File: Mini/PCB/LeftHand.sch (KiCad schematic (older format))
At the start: 30 parts

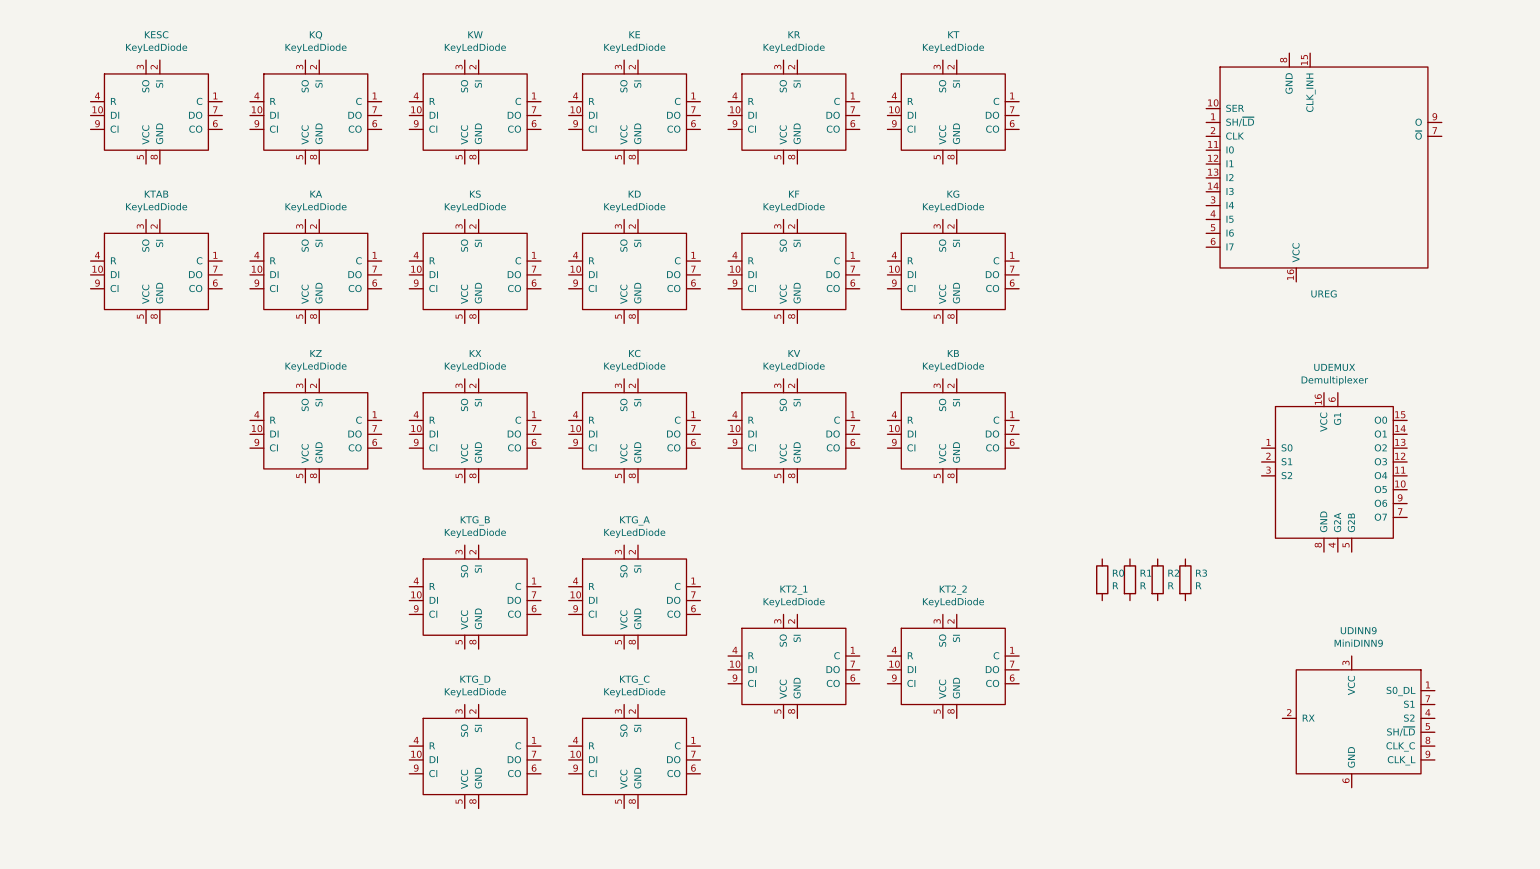
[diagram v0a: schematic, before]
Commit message: Wiring left hand schematic, adding footprints, and generating netlist.
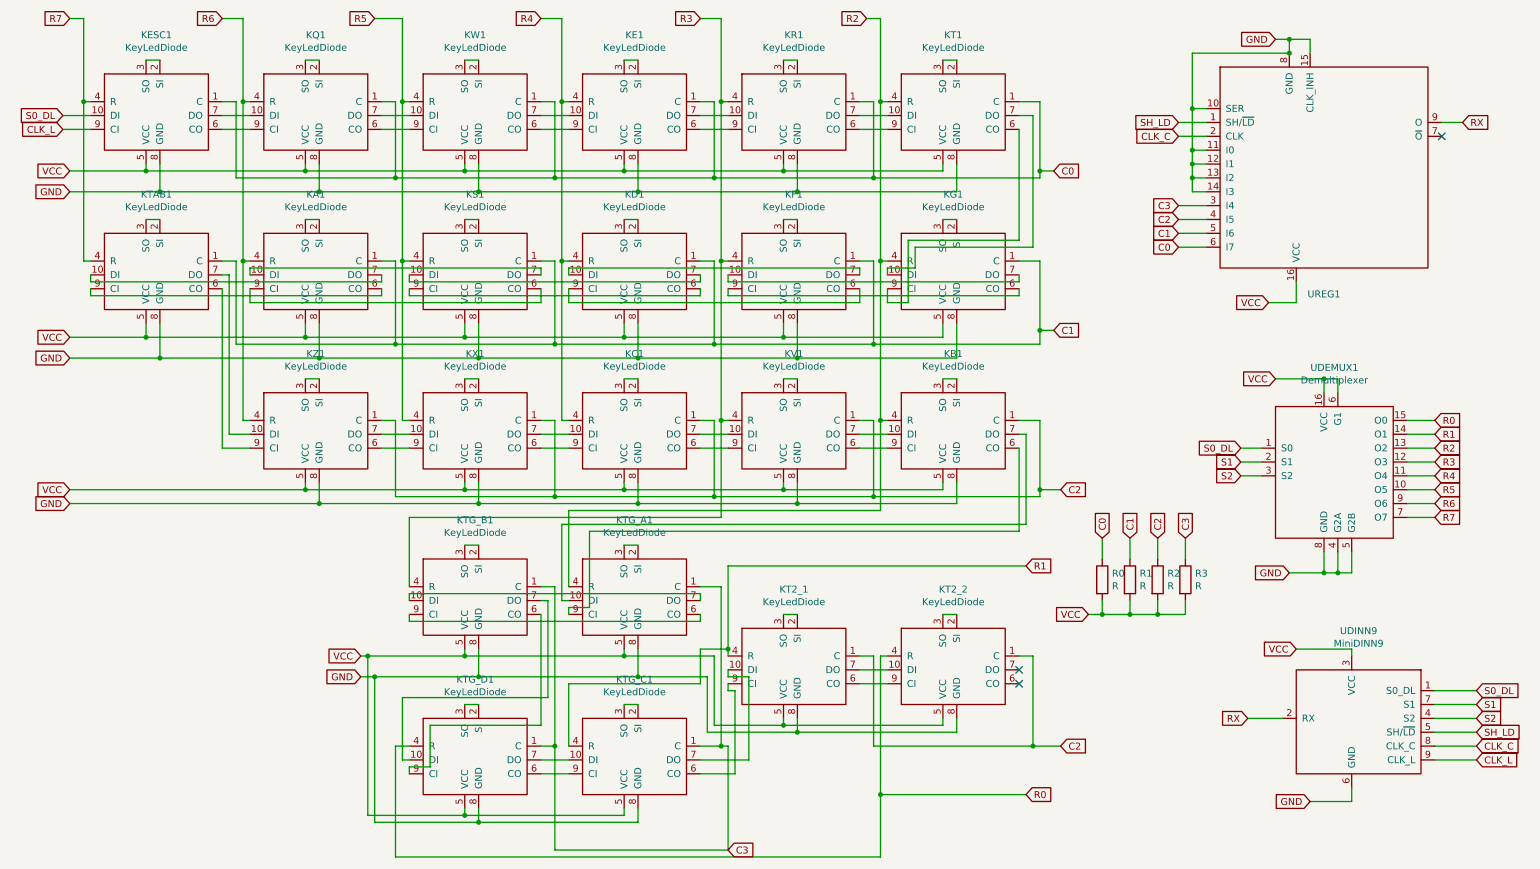
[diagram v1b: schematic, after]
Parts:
- KA1: renamed from KA; footprint (none) -> Mini:KeyLedDiodeR2L
- KB1: renamed from KB; footprint (none) -> Mini:KeyLedDiodeL2R
- KC1: renamed from KC; footprint (none) -> Mini:KeyLedDiodeL2R
- KD1: renamed from KD; footprint (none) -> Mini:KeyLedDiodeR2L
- KE1: renamed from KE; footprint (none) -> Mini:KeyLedDiodeL2R
- KESC1: renamed from KESC; footprint (none) -> Mini:KeyLedDiodeL2R
- KF1: renamed from KF; footprint (none) -> Mini:KeyLedDiodeR2L
- KG1: renamed from KG; footprint (none) -> Mini:KeyLedDiodeR2L
- KQ1: renamed from KQ; footprint (none) -> Mini:KeyLedDiodeL2R
- KR1: renamed from KR; footprint (none) -> Mini:KeyLedDiodeL2R
- KS1: renamed from KS; footprint (none) -> Mini:KeyLedDiodeR2L
- KT1: renamed from KT; footprint (none) -> Mini:KeyLedDiodeL2R
- KT2_1: footprint (none) -> Mini:Key2LedDiodeR2L
- KT2_2: footprint (none) -> Mini:Key2LedDiodeL2R
- KTAB1: renamed from KTAB; footprint (none) -> Mini:KeyLedDiodeR2L
- KTG_A1: renamed from KTG_A; footprint (none) -> Mini:KeyLedDiodeR2L
- KTG_B1: renamed from KTG_B; footprint (none) -> Mini:KeyLedDiodeR2L
- KTG_C1: renamed from KTG_C; footprint (none) -> Mini:KeyLedDiodeL2R
- KTG_D1: renamed from KTG_D; footprint (none) -> Mini:KeyLedDiodeL2R
- KV1: renamed from KV; footprint (none) -> Mini:KeyLedDiodeL2R
- KW1: renamed from KW; footprint (none) -> Mini:KeyLedDiodeL2R
- KX1: renamed from KX; footprint (none) -> Mini:KeyLedDiodeL2R
- KZ1: renamed from KZ; footprint (none) -> Mini:KeyLedDiodeL2R
- R0, R1, R2, R3: footprint (none) -> Mini:PullupResistor
- UDEMUX1: renamed from UDEMUX; footprint (none) -> Mini:DualInlineMicrochip2x8
- UDINN9: footprint (none) -> Mini:MiniDin9
- UREG1: renamed from UREG; footprint (none) -> Mini:DualInlineMicrochip2x8
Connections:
- net S0_DL: now reaches UDINN9.1 (S0_DL)
- net S0_DL: now also KESC1.10 (DI), UDEMUX1.1 (S0)
- net RX: now reaches UDINN9.2 (RX)
- net RX: now also UREG1.9 (O)
- net VCC: now reaches UDINN9.3 (VCC)
- net VCC: now also KA1.5 (VCC), KB1.5 (VCC), KC1.5 (VCC), KD1.5 (VCC), KE1.5 (VCC), KESC1.5 (VCC), KF1.5 (VCC), KG1.5 (VCC), KQ1.5 (VCC), KR1.5 (VCC), KS1.5 (VCC), KT1.5 (VCC), KT2_1.5 (VCC), KT2_2.5 (VCC), KTAB1.5 (VCC), KTG_A1.5 (VCC), KTG_B1.5 (VCC), KTG_C1.5 (VCC), KTG_D1.5 (VCC), KV1.5 (VCC), KW1.5 (VCC), KX1.5 (VCC), KZ1.5 (VCC), R0.2, R1.2, R2.2, R3.2, UDEMUX1.16 (VCC), UDEMUX1.6 (G1), UREG1.16 (VCC)
- net S2: now reaches UDINN9.4 (S2)
- net S2: now also UDEMUX1.3 (S2)
- net SH_LD: now reaches UDINN9.5 (SH/~LD)
- net SH_LD: now also UREG1.1 (SH/~LD)
- net GND: now reaches UDINN9.6 (GND)
- net GND: now also KA1.8 (GND), KB1.8 (GND), KC1.8 (GND), KD1.8 (GND), KE1.8 (GND), KESC1.8 (GND), KF1.8 (GND), KG1.8 (GND), KQ1.8 (GND), KR1.8 (GND), KS1.8 (GND), KT1.8 (GND), KT2_1.8 (GND), KT2_2.8 (GND), KTAB1.8 (GND), KTG_A1.8 (GND), KTG_B1.8 (GND), KTG_C1.8 (GND), KTG_D1.8 (GND), KV1.8 (GND), KW1.8 (GND), KX1.8 (GND), KZ1.8 (GND), UDEMUX1.4 (G2A), UDEMUX1.5 (G2B), UDEMUX1.8 (GND), UREG1.10 (SER), UREG1.11 (I0), UREG1.12 (I1), UREG1.13 (I2), UREG1.14 (I3), UREG1.15 (CLK_INH), UREG1.8 (GND)
- net S1: now reaches UDINN9.7 (S1)
- net S1: now also UDEMUX1.2 (S1)
- net CLK_C: now reaches UDINN9.8 (CLK_C)
- net CLK_C: now also UREG1.2 (CLK)
- net CLK_L: now reaches UDINN9.9 (CLK_L)
- net CLK_L: now also KESC1.9 (CI)
- net R5: now reaches UDEMUX1.10 (O5)
- net R5: now also KS1.4 (R), KW1.4 (R), KX1.4 (R)
- net R4: now reaches UDEMUX1.11 (O4)
- net R4: now also KC1.4 (R), KD1.4 (R), KE1.4 (R)
- net R3: now reaches UDEMUX1.12 (O3)
- net R3: now also KF1.4 (R), KR1.4 (R), KTG_B1.4 (R), KV1.4 (R)
- net R2: now reaches UDEMUX1.13 (O2)
- net R2: now also KB1.4 (R), KG1.4 (R), KT1.4 (R), KTG_A1.4 (R)
- net R1: now reaches UDEMUX1.14 (O1)
- net R1: now also KT2_1.4 (R), KTG_C1.4 (R)
- net R0: now reaches UDEMUX1.15 (O0)
- net R0: now also KT2_2.4 (R), KTG_D1.4 (R)
- net R7: now reaches UDEMUX1.7 (O7)
- net R7: now also KESC1.4 (R), KTAB1.4 (R)
- net R6: now reaches UDEMUX1.9 (O6)
- net R6: now also KA1.4 (R), KQ1.4 (R), KZ1.4 (R)
- net C3: now reaches UREG1.3 (I4)
- net C3: now also KTG_A1.1 (C), KTG_B1.1 (C), KTG_C1.1 (C), KTG_D1.1 (C), R3.1
- net C2: now reaches UREG1.4 (I5)
- net C2: now also KB1.1 (C), KC1.1 (C), KT2_1.1 (C), KT2_2.1 (C), KV1.1 (C), KX1.1 (C), KZ1.1 (C), R2.1
- net C1: now reaches UREG1.5 (I6)
- net C1: now also KA1.1 (C), KD1.1 (C), KF1.1 (C), KG1.1 (C), KS1.1 (C), KTAB1.1 (C), R1.1
- net C0: now reaches UREG1.6 (I7)
- net C0: now also KE1.1 (C), KESC1.1 (C), KQ1.1 (C), KR1.1 (C), KT1.1 (C), KW1.1 (C), R0.1
- net at KESC1.2 (SI): now also KESC1.3 (SO)
- net at KESC1.6 (CO): now also KQ1.9 (CI)
- net at KESC1.7 (DO): now also KQ1.10 (DI)
- net at KQ1.2 (SI): now also KQ1.3 (SO)
- net at KQ1.6 (CO): now also KW1.9 (CI)
- net at KQ1.7 (DO): now also KW1.10 (DI)
- net at KW1.2 (SI): now also KW1.3 (SO)
- net at KW1.6 (CO): now also KE1.9 (CI)
- net at KW1.7 (DO): now also KE1.10 (DI)
- net at KE1.2 (SI): now also KE1.3 (SO)
- net at KE1.6 (CO): now also KR1.9 (CI)
- net at KE1.7 (DO): now also KR1.10 (DI)
- net at KR1.2 (SI): now also KR1.3 (SO)
- net at KR1.6 (CO): now also KT1.9 (CI)
- net at KR1.7 (DO): now also KT1.10 (DI)
- net at KT1.2 (SI): now also KT1.3 (SO)
- net at KT1.6 (CO): now also KG1.9 (CI)
- net at KT1.7 (DO): now also KG1.10 (DI)
- net at KTAB1.10 (DI): now also KA1.7 (DO)
- net at KTAB1.2 (SI): now also KTAB1.3 (SO)
- net at KTAB1.6 (CO): now also KZ1.9 (CI)
- net at KTAB1.7 (DO): now also KZ1.10 (DI)
- net at KTAB1.9 (CI): now also KA1.6 (CO)
- net at KA1.10 (DI): now also KS1.7 (DO)
- net at KA1.2 (SI): now also KA1.3 (SO)
- net at KA1.9 (CI): now also KS1.6 (CO)
- net at KS1.10 (DI): now also KD1.7 (DO)
- net at KS1.2 (SI): now also KS1.3 (SO)
- net at KS1.9 (CI): now also KD1.6 (CO)
- net at KD1.10 (DI): now also KF1.7 (DO)
- net at KD1.2 (SI): now also KD1.3 (SO)
- net at KD1.9 (CI): now also KF1.6 (CO)
- net at KF1.10 (DI): now also KG1.7 (DO)
- net at KF1.2 (SI): now also KF1.3 (SO)
- net at KF1.9 (CI): now also KG1.6 (CO)
- net at KG1.2 (SI): now also KG1.3 (SO)
- net at KZ1.2 (SI): now also KZ1.3 (SO)
- net at KZ1.6 (CO): now also KX1.9 (CI)
- net at KZ1.7 (DO): now also KX1.10 (DI)
- net at KX1.2 (SI): now also KX1.3 (SO)
- net at KX1.6 (CO): now also KC1.9 (CI)
- net at KX1.7 (DO): now also KC1.10 (DI)
- net at KC1.2 (SI): now also KC1.3 (SO)
- net at KC1.6 (CO): now also KV1.9 (CI)
- net at KC1.7 (DO): now also KV1.10 (DI)
- net at KV1.2 (SI): now also KV1.3 (SO)
- net at KV1.6 (CO): now also KB1.9 (CI)
- net at KV1.7 (DO): now also KB1.10 (DI)
- net at KB1.2 (SI): now also KB1.3 (SO)
- net at KB1.6 (CO): now also KTG_A1.9 (CI)
- net at KB1.7 (DO): now also KTG_A1.10 (DI)
- net at KT2_2.10 (DI): now also KT2_1.7 (DO)
- net at KT2_2.2 (SI): now also KT2_2.3 (SO)
- net at KT2_2.9 (CI): now also KT2_1.6 (CO)
- net at KT2_1.10 (DI): now also KTG_C1.7 (DO)
- net at KT2_1.2 (SI): now also KT2_1.3 (SO)
- net at KT2_1.9 (CI): now also KTG_C1.6 (CO)
- net at KTG_A1.2 (SI): now also KTG_A1.3 (SO)
- net at KTG_A1.6 (CO): now also KTG_B1.9 (CI)
- net at KTG_A1.7 (DO): now also KTG_B1.10 (DI)
- net at KTG_C1.10 (DI): now also KTG_D1.7 (DO)
- net at KTG_C1.2 (SI): now also KTG_C1.3 (SO)
- net at KTG_C1.9 (CI): now also KTG_D1.6 (CO)
- net at KTG_B1.2 (SI): now also KTG_B1.3 (SO)
- net at KTG_B1.6 (CO): now also KTG_D1.9 (CI)
- net at KTG_B1.7 (DO): now also KTG_D1.10 (DI)
- net at KTG_D1.2 (SI): now also KTG_D1.3 (SO)
- no-connect marks 0 -> 3

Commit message: Adding components to PCB.  Fixing T2 footprints.  Still need wiring and holes.
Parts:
- KT2_1: footprint Mini:Key2LedDiodeR2L -> Mini:Key2LedDiodeL2R
- KT2_2: footprint Mini:Key2LedDiodeL2R -> Mini:Key2LedDiodeR2L
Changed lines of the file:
@@
 F 0 "KT2_2" H 7075 5781 50  0000 C CNN
 F 1 "KeyLedDiode" H 7075 5690 50  0000 C CNN
-F 2 "Mini:Key2LedDiodeL2R" H 7100 5250 50  0001 C CNN
+F 2 "Mini:Key2LedDiodeR2L" H 7100 5250 50  0001 C CNN
 F 3 "" H 7100 5250 50  0001 C CNN
 	1    7100 5250
@@
 F 0 "KT2_1" H 5925 5781 50  0000 C CNN
 F 1 "KeyLedDiode" H 5925 5690 50  0000 C CNN
-F 2 "Mini:Key2LedDiodeR2L" H 5950 5250 50  0001 C CNN
+F 2 "Mini:Key2LedDiodeL2R" H 5950 5250 50  0001 C CNN
 F 3 "" H 5950 5250 50  0001 C CNN
 	1    5950 5250
